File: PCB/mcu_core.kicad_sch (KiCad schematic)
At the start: 13 parts

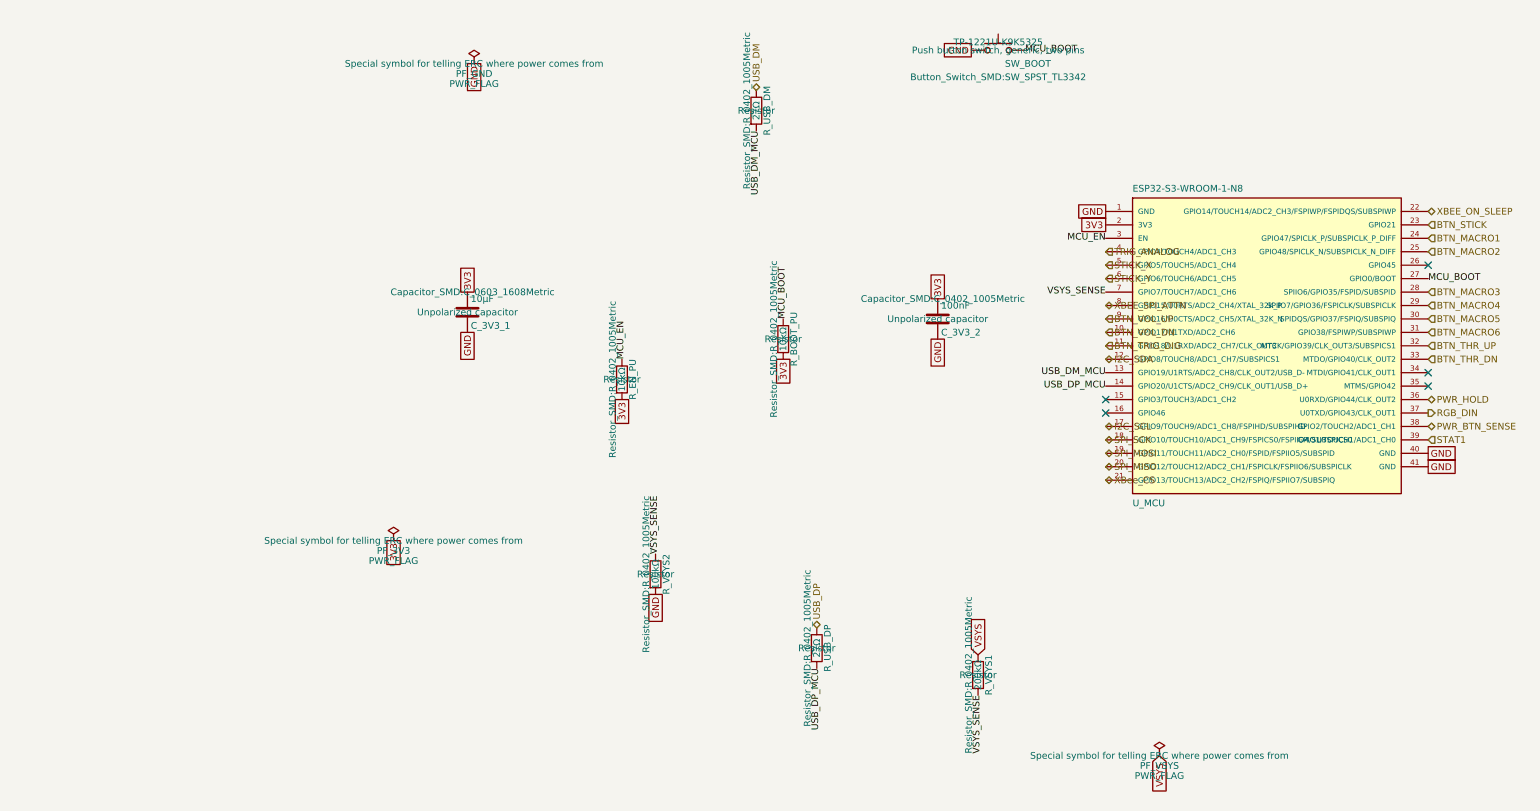
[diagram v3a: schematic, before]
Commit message: layout: everything is on the board
The board edge cuts are down to 100mm x 35mm. All the components have the right footprints and are on the board, but no traces exist yet, and not all circuits are laid out properly yet. Lots of DRC warnings.
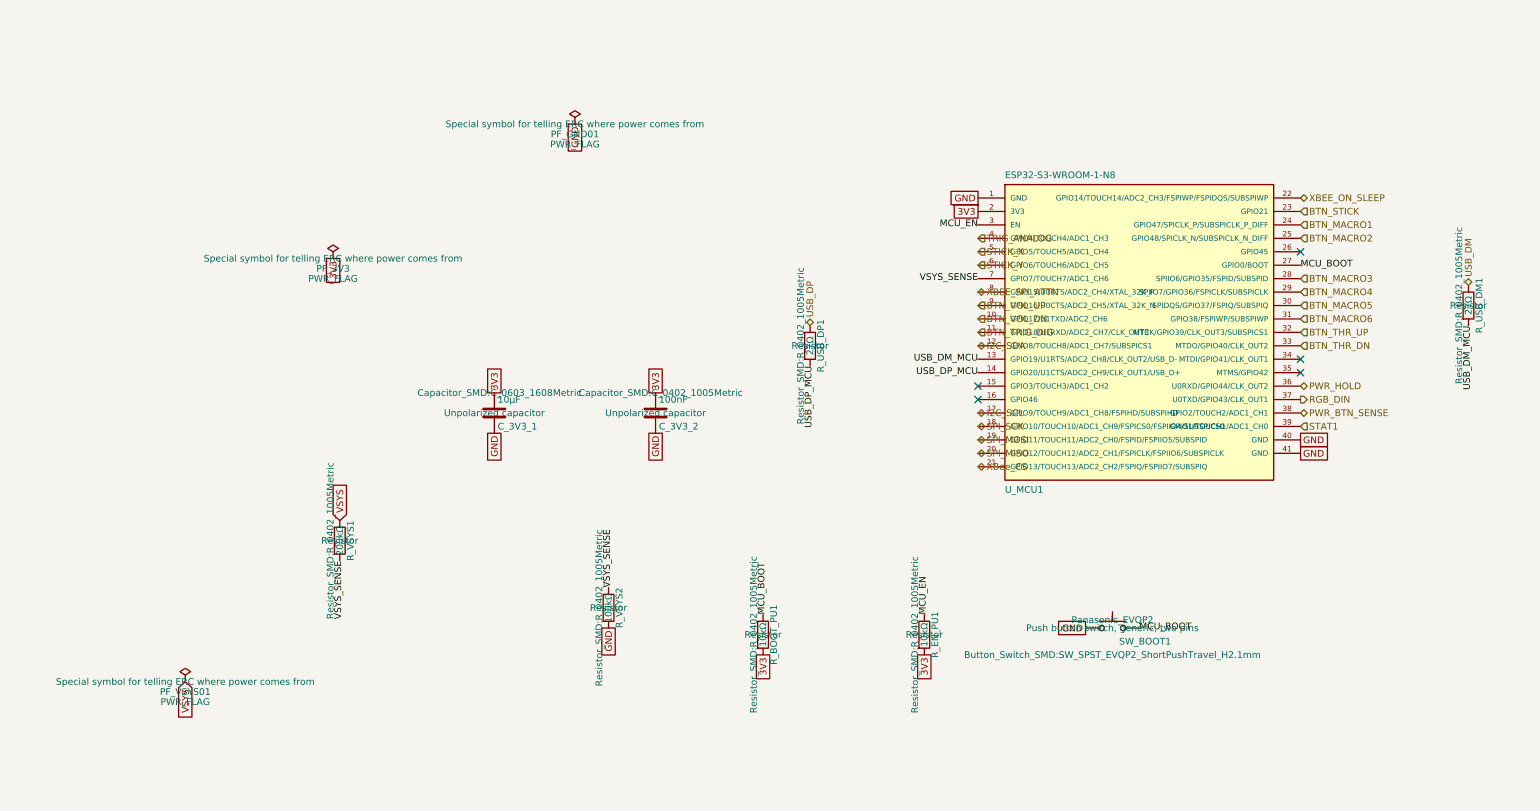
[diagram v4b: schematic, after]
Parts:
- removed PF_3V3, PF_GND, PF_VSYS: PWR_FLAG, symbol power:PWR_FLAG
- removed R_BOOT_PU, R_EN_PU: 10kΩ, Resistor_SMD:R_0402_1005Metric, symbol Device:R
- removed R_USB_DM, R_USB_DP: 27Ω, Resistor_SMD:R_0402_1005Metric, symbol Device:R
- removed SW_BOOT: TP-1221U-K9K5325, Button_Switch_SMD:SW_SPST_TL3342, symbol Switch:SW_Push
- removed U_MCU: ESP32-S3-WROOM-1-N8, Espressif:ESP32-S3-WROOM-1, symbol Espressif:ESP32-S3-WROOM-1
- added R_BOOT_PU1, R_EN_PU1: 10kΩ, Resistor_SMD:R_0402_1005Metric, symbol Device:R
- added R_USB_DM1, R_USB_DP1: 27Ω, Resistor_SMD:R_0402_1005Metric, symbol Device:R
- added SW_BOOT1: Panasonic_EVQP2, Button_Switch_SMD:SW_SPST_EVQP2_ShortPushTravel_H2.1mm, symbol Switch:SW_Push
- added U_MCU1: ESP32-S3-WROOM-1-N8, Espressif:ESP32-S3-WROOM-1, symbol Espressif:ESP32-S3-WROOM-1
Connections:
- net 3V3: now also R_BOOT_PU1.2, R_EN_PU1.2, U_MCU1.2 (3V3)
- net BTN_MACRO1: now also U_MCU1.24 (GPIO47/SPICLK_P/SUBSPICLK_P_DIFF)
- net BTN_MACRO2: now also U_MCU1.25 (GPIO48/SPICLK_N/SUBSPICLK_N_DIFF)
- net BTN_MACRO3: now also U_MCU1.28 (SPIIO6/GPIO35/FSPID/SUBSPID)
- net BTN_MACRO4: now also U_MCU1.29 (SPIIO7/GPIO36/FSPICLK/SUBSPICLK)
- net BTN_MACRO5: now also U_MCU1.30 (SPIDQS/GPIO37/FSPIQ/SUBSPIQ)
- net BTN_MACRO6: now also U_MCU1.31 (GPIO38/FSPIWP/SUBSPIWP)
- net BTN_STICK: now also U_MCU1.23 (GPIO21)
- net BTN_THR_DN: now also U_MCU1.33 (MTDO/GPIO40/CLK_OUT2)
- net BTN_THR_UP: now also U_MCU1.32 (MTCK/GPIO39/CLK_OUT3/SUBSPICS1)
- net BTN_TRIG_DIG: now also U_MCU1.11 (GPIO18/U1RXD/ADC2_CH7/CLK_OUT3)
- net BTN_VOL_DN: now also U_MCU1.10 (GPIO17/U1TXD/ADC2_CH6)
- net BTN_VOL_UP: now also U_MCU1.9 (GPIO16/U0CTS/ADC2_CH5/XTAL_32K_N)
- net GND: now also SW_BOOT1.1, U_MCU1.1 (GND), U_MCU1.40 (GND), U_MCU1.41 (GND)
- net I2C_SCL: now also U_MCU1.17 (GPIO9/TOUCH9/ADC1_CH8/FSPIHD/SUBSPIHD)
- net I2C_SDA: now also U_MCU1.12 (GPIO8/TOUCH8/ADC1_CH7/SUBSPICS1)
- net MCU_BOOT: now also R_BOOT_PU1.1, SW_BOOT1.2, U_MCU1.27 (GPIO0/BOOT)
- net MCU_EN: now also R_EN_PU1.1, U_MCU1.3 (EN)
- net PWR_BTN_SENSE: now also U_MCU1.38 (GPIO2/TOUCH2/ADC1_CH1)
- net PWR_HOLD: now also U_MCU1.36 (U0RXD/GPIO44/CLK_OUT2)
- net RGB_DIN: now also U_MCU1.37 (U0TXD/GPIO43/CLK_OUT1)
- net SPI_MISO: now also U_MCU1.20 (GPIO12/TOUCH12/ADC2_CH1/FSPICLK/FSPIIO6/SUBSPICLK)
- net SPI_MOSI: now also U_MCU1.19 (GPIO11/TOUCH11/ADC2_CH0/FSPID/FSPIIO5/SUBSPID)
- net SPI_SCK: now also U_MCU1.18 (GPIO10/TOUCH10/ADC1_CH9/FSPICS0/FSPIIO4/SUBSPICS0)
- net STAT1: now also U_MCU1.39 (GPIO1/TOUCH1/ADC1_CH0)
- net STICK_X: now also U_MCU1.5 (GPIO5/TOUCH5/ADC1_CH4)
- net STICK_Y: now also U_MCU1.6 (GPIO6/TOUCH6/ADC1_CH5)
- net TRIG_ANALOG: now also U_MCU1.4 (GPIO4/TOUCH4/ADC1_CH3)
- net USB_DM: now also R_USB_DM1.1
- net USB_DM_MCU: now also R_USB_DM1.2, U_MCU1.13 (GPIO19/U1RTS/ADC2_CH8/CLK_OUT2/USB_D-)
- net USB_DP: now also R_USB_DP1.1
- net USB_DP_MCU: now also R_USB_DP1.2, U_MCU1.14 (GPIO20/U1CTS/ADC2_CH9/CLK_OUT1/USB_D+)
- net VSYS_SENSE: now also U_MCU1.7 (GPIO7/TOUCH7/ADC1_CH6)
- net XBEE_ON_SLEEP: now also U_MCU1.22 (GPIO14/TOUCH14/ADC2_CH3/FSPIWP/FSPIDQS/SUBSPIWP)
- net XBEE_SPI_ATTN: now also U_MCU1.8 (GPIO15/U0RTS/ADC2_CH4/XTAL_32K_P)
- net XBee_CS: now also U_MCU1.21 (GPIO13/TOUCH13/ADC2_CH2/FSPIQ/FSPIIO7/SUBSPIQ)

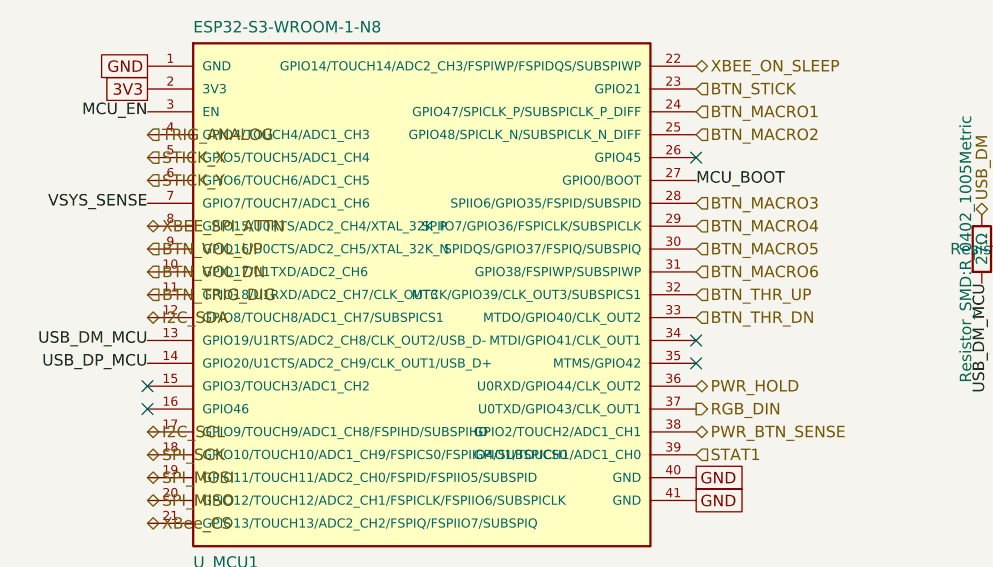
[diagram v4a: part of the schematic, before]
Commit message: task: board is fully routed
That was a pain, but it is all routed and connected now.
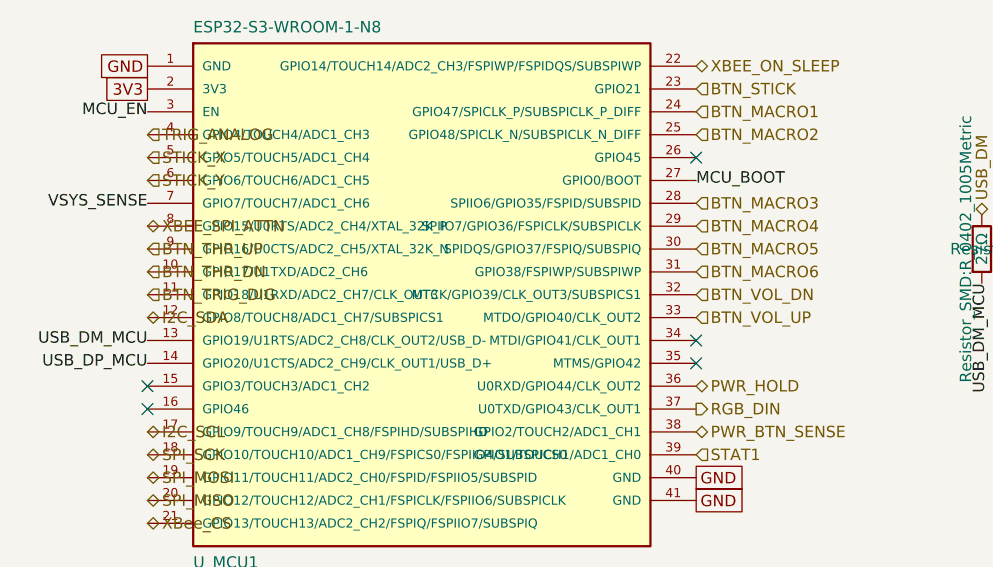
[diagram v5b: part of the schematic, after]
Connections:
- net BTN_THR_DN: now also U_MCU1.10 (GPIO17/U1TXD/ADC2_CH6); no longer U_MCU1.33 (MTDO/GPIO40/CLK_OUT2)
- net BTN_THR_UP: now also U_MCU1.9 (GPIO16/U0CTS/ADC2_CH5/XTAL_32K_N); no longer U_MCU1.32 (MTCK/GPIO39/CLK_OUT3/SUBSPICS1)
- net BTN_VOL_DN: now also U_MCU1.32 (MTCK/GPIO39/CLK_OUT3/SUBSPICS1); no longer U_MCU1.10 (GPIO17/U1TXD/ADC2_CH6)
- net BTN_VOL_UP: now also U_MCU1.33 (MTDO/GPIO40/CLK_OUT2); no longer U_MCU1.9 (GPIO16/U0CTS/ADC2_CH5/XTAL_32K_N)
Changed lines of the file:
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@@
 		)
 	)
-	(hierarchical_label "BTN_VOL_DN"
+	(hierarchical_label "BTN_THR_DN"
 		(shape input)
 		(at 176.53 88.9 0)
@@
 		)
 	)
-	(hierarchical_label "BTN_THR_DN"
+	(hierarchical_label "BTN_VOL_UP"
 		(shape input)
 		(at 237.49 93.98 0)
@@
 		)
 	)
-	(hierarchical_label "BTN_VOL_UP"
+	(hierarchical_label "BTN_THR_UP"
 		(shape input)
 		(at 176.53 86.36 0)
@@
 		)
 	)
-	(hierarchical_label "BTN_THR_UP"
+	(hierarchical_label "BTN_VOL_DN"
 		(shape input)
 		(at 237.49 91.44 0)

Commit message: task: first validation pass
This is the results post first kicad-happy run.
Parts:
- added C_3V3_3: 39pF, Capacitor_SMD:C_0402_1005Metric, symbol Device:C
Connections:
- net 3V3: now also C_3V3_3.1
- net GND: now also C_3V3_3.2

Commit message: task: part number populated (#26)
kicad-happy run part 2 - MPN numbers populated
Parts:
- C_3V3_1: MF (none) -> Yageo; Manufacturer_Part_Number (none) -> CC0603KRX5R7BB106
- C_3V3_2: MF (none) -> Yageo; Manufacturer_Part_Number (none) -> CC0402KRX7R9BB104
- C_3V3_3: MF (none) -> Yageo; Manufacturer_Part_Number (none) -> CC0402JRNPO9BN390
- R_BOOT_PU1, R_EN_PU1: MF (none) -> Yageo; Manufacturer_Part_Number (none) -> RC0402FR-0710KL
- R_USB_DM1, R_USB_DP1: MF (none) -> Yageo; Manufacturer_Part_Number (none) -> RC0402FR-0727RL
- R_VSYS1: MF (none) -> Yageo; Manufacturer_Part_Number (none) -> RC0402FR-07200KL
- R_VSYS2: MF (none) -> Yageo; Manufacturer_Part_Number (none) -> RC0402FR-07100KL
- SW_BOOT1: MF (none) -> Panasonic; Manufacturer_Part_Number (none) -> EVQP2T02M
- U_MCU1: Manufacturer_Part_Number (none) -> ESP32-S3-WROOM-1-N8
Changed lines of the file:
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@@
+			)
+		)
+		(property "MF" "Yageo" (at 0 0 0)
+			(effects
+				(font
+					(size 1.27 1.27)
+				)
+				(hide yes)
+			)
+		)
+		(property "Manufacturer_Part_Number" "CC0603KRX5R7BB106" (at 0 0 0)
+			(effects
+				(font
+					(size 1.27 1.27)
+				)
+				(hide yes)
 			)
 		)
@@
 			)
 		)
+		(property "Manufacturer_Part_Number" "ESP32-S3-WROOM-1-N8" (at 0 0 0)
+			(effects
+				(font
+					(size 1.27 1.27)
+				)
+				(hide yes)
+			)
+		)
 		(pin "1"
 		)
@@
 			)
 		)
+		(property "MF" "Yageo" (at 0 0 0)
+			(effects
+				(font
+					(size 1.27 1.27)
+				)
+				(hide yes)
+			)
+		)
+		(property "Manufacturer_Part_Number" "RC0402FR-0710KL" (at 0 0 0)
+			(effects
+				(font
+					(size 1.27 1.27)
+				)
+				(hide yes)
+			)
+		)
 		(pin "1"
 		)
@@
 			)
 		)
+		(property "MF" "Yageo" (at 0 0 0)
+			(effects
+				(font
+					(size 1.27 1.27)
+				)
+				(hide yes)
+			)
+		)
+		(property "Manufacturer_Part_Number" "CC0402JRNPO9BN390" (at 0 0 0)
+			(effects
+				(font
+					(size 1.27 1.27)
+				)
+				(hide yes)
+			)
+		)
 		(pin "1"
 		)
@@
 			)
 		)
+		(property "MF" "Yageo" (at 0 0 0)
+			(effects
+				(font
+					(size 1.27 1.27)
+				)
+				(hide yes)
+			)
+		)
+		(property "Manufacturer_Part_Number" "RC0402FR-0710KL" (at 0 0 0)
+			(effects
+				(font
+					(size 1.27 1.27)
+				)
+				(hide yes)
+			)
+		)
 		(pin "1"
 		)
@@
 			)
 		)
+		(property "MF" "Yageo" (at 0 0 0)
+			(effects
+				(font
+					(size 1.27 1.27)
+				)
+				(hide yes)
+			)
+		)
+		(property "Manufacturer_Part_Number" "RC0402FR-07200KL" (at 0 0 0)
+			(effects
+				(font
+					(size 1.27 1.27)
+				)
+				(hide yes)
+			)
+		)
 		(pin "1"
 		)
@@
 			)
 		)
+		(property "Manufacturer_Part_Number" "EVQP2T02M" (at 0 0 0)
+			(effects
+				(font
+					(size 1.27 1.27)
+				)
+				(hide yes)
+			)
+		)
+		(property "MF" "Panasonic" (at 0 0 0)
+			(effects
+				(font
+					(size 1.27 1.27)
+				)
+				(hide yes)
+			)
+		)
 		(pin "1"
 		)
@@
 			)
 		)
+		(property "MF" "Yageo" (at 0 0 0)
+			(effects
+				(font
+					(size 1.27 1.27)
+				)
+				(hide yes)
+			)
+		)
+		(property "Manufacturer_Part_Number" "RC0402FR-0727RL" (at 0 0 0)
+			(effects
+				(font
+					(size 1.27 1.27)
+				)
+				(hide yes)
+			)
+		)
 		(pin "1"
 		)
@@
 			)
 		)
+		(property "MF" "Yageo" (at 0 0 0)
+			(effects
+				(font
+					(size 1.27 1.27)
+				)
+				(hide yes)
+			)
+		)
+		(property "Manufacturer_Part_Number" "RC0402FR-07100KL" (at 0 0 0)
+			(effects
+				(font
+					(size 1.27 1.27)
+				)
+				(hide yes)
+			)
+		)
 		(pin "1"
 		)
@@
 			)
 		)
+		(property "MF" "Yageo" (at 0 0 0)
+			(effects
+				(font
+					(size 1.27 1.27)
+				)
+				(hide yes)
+			)
+		)
+		(property "Manufacturer_Part_Number" "CC0402KRX7R9BB104" (at 0 0 0)
+			(effects
+				(font
+					(size 1.27 1.27)
+				)
+				(hide yes)
+			)
+		)
 		(pin "1"
 		)
@@
 			)
 		)
+		(property "MF" "Yageo" (at 0 0 0)
+			(effects
+				(font
+					(size 1.27 1.27)
+				)
+				(hide yes)
+			)
+		)
+		(property "Manufacturer_Part_Number" "RC0402FR-0727RL" (at 0 0 0)
+			(effects
+				(font
+					(size 1.27 1.27)
+				)
+				(hide yes)
+			)
+		)
